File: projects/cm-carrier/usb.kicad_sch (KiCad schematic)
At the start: 37 parts, among them J3 USB_C_HOST (USB2.0), J4 XA_USB1, J5 XA_USB2, U2 USB2514B-I/M2, U3 TPS2051CDBV, U4 TPS2051CDBV, U5 TPS2051CDBV, U6 USBLC6-2SC6, U7 USBLC6-2SC6, U8 USBLC6-2SC6, Y1 24MHz CL=18pF

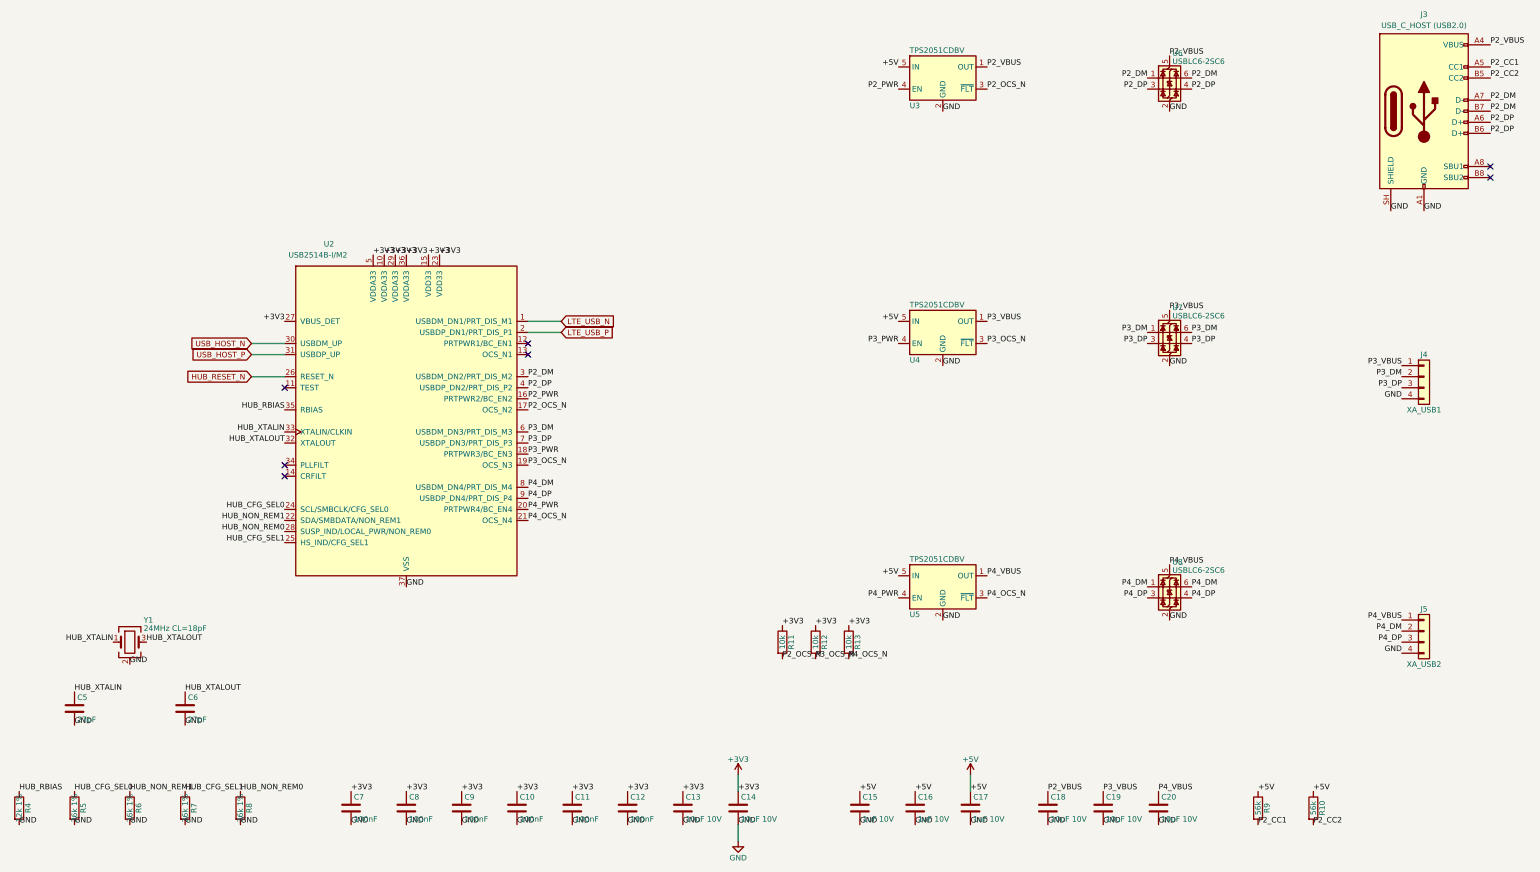
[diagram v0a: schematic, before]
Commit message: cm-carrier: schematic readability cleanup (no netlist change)
Co-Authored-By: Claude Opus 5.5 <noreply@anthropic.com>
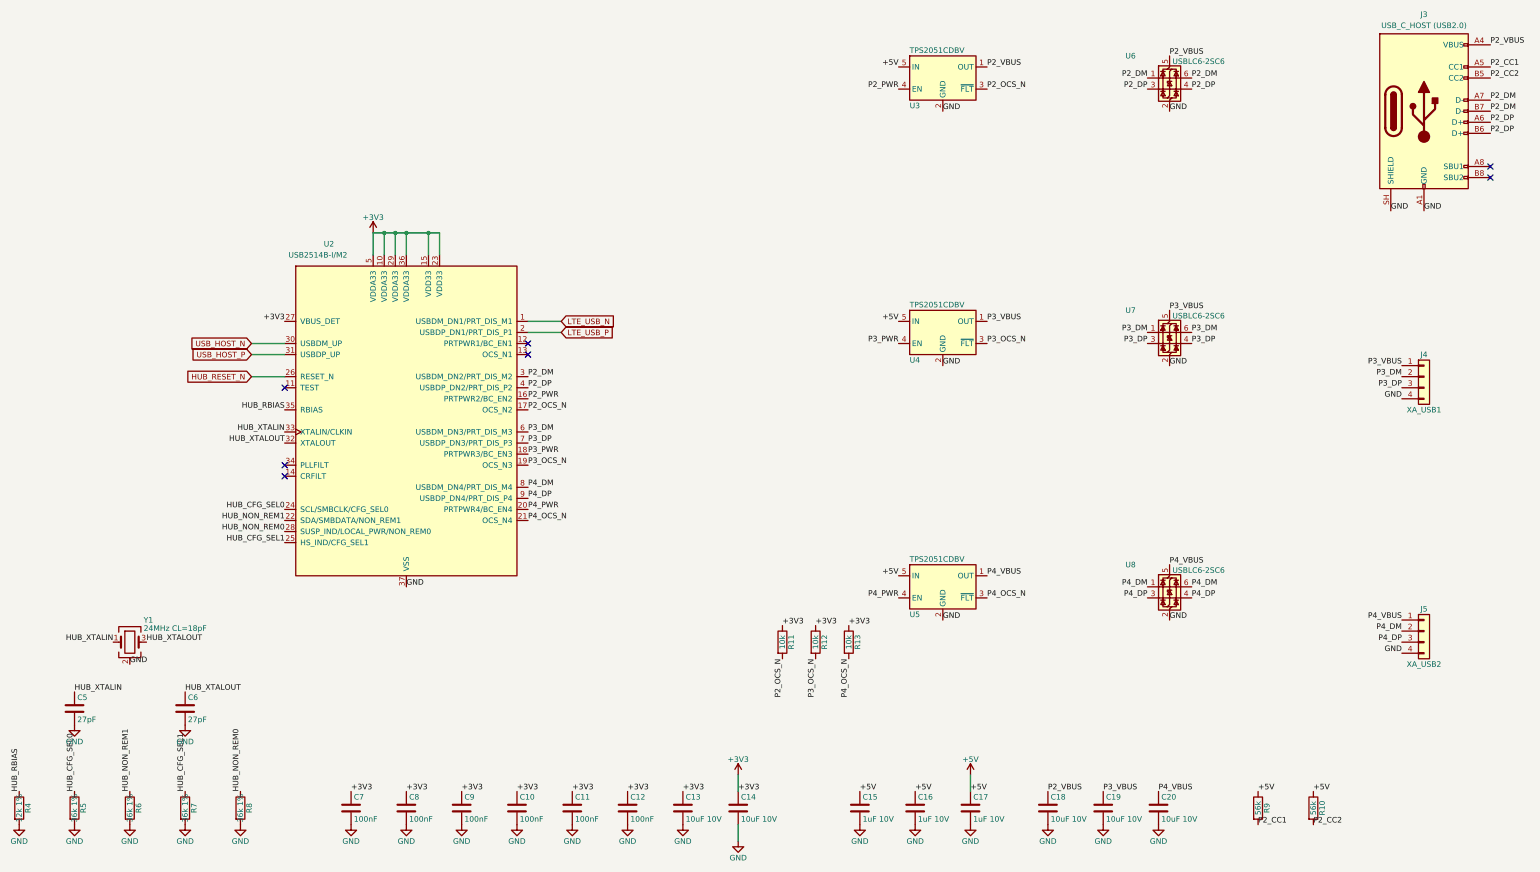
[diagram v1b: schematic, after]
